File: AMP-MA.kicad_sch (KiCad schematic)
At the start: 51 parts, among them Q1 2N5484, Q12 2N5484, Q13 2N5484, Q2 2N5484, U2 LM1875

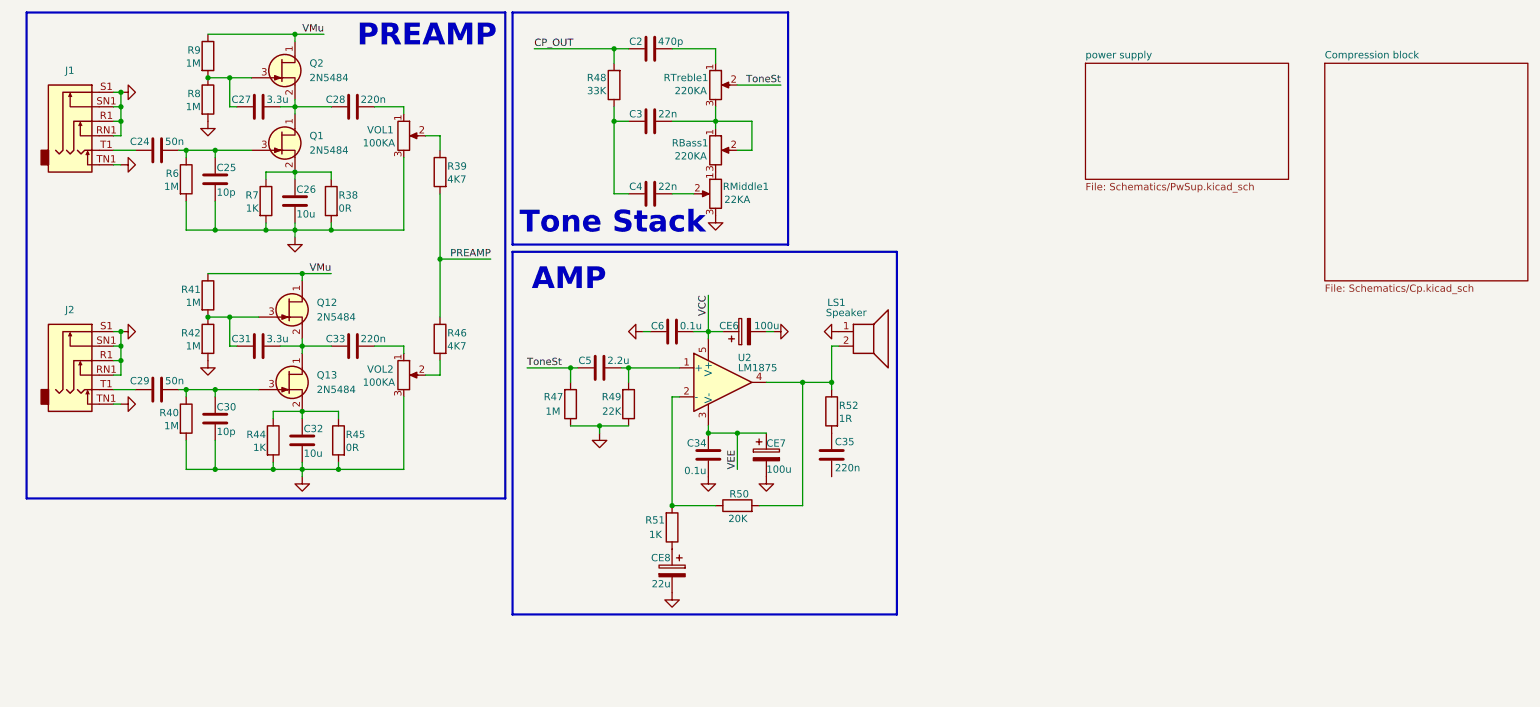
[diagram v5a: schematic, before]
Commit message: directory cleared, Schem upd
The input mixer changed from passive to active(TL072)
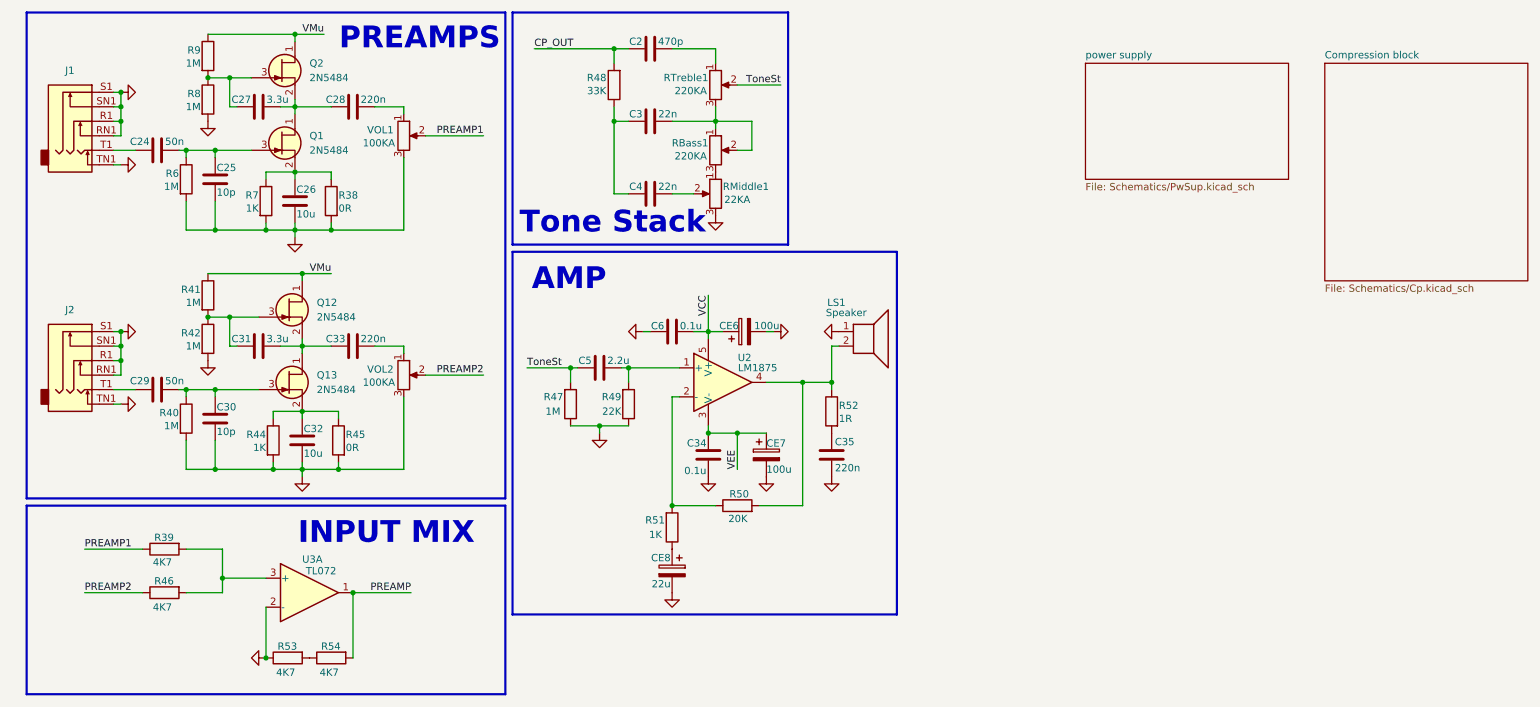
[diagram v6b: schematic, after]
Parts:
- added R53, R54: 4K7, Resistor_THT:R_Axial_DIN0207_L6.3mm_D2.5mm_P10.16mm_Horizontal, symbol Device:R
- added U3: TL072, symbol Amplifier_Operational:TL072
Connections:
- net GND: now also C35.2, R53.1, U3.2 (-)
- net PREAMP: now also R54.2, U3.1; no longer R39.2, R46.1
- net PREAMP1: now reaches R39.1, VOL1.2
- net at R46.2: now also R39.2, U3.3 (+); no longer VOL2.2
- new net: R53.2, R54.1
- new net PREAMP2: R46.1, VOL2.2
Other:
- note added: "INPUT MIX"
- note added: "PREAMPS"
- note removed: "PREAMP"

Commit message: Schem upd & added .gitignore
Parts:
- added J8: Conn_01x05_Socket, symbol Connector:Conn_01x05_Socket
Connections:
- net GND: now also CE7.1; no longer CE7.2
- net VCC: now also J8.4 (Pin_4)
- net VEE: now also CE7.2, J8.3 (Pin_3); no longer CE7.1
- net LM_OUT: now reaches LS1.2, R50.2, R52.1, U2.4
- net LM_OUT: now also J8.5 (Pin_5)
- net LM_IN-: now reaches R50.1, R51.2, U2.2 (-)
- net LM_IN-: now also J8.1 (Pin_1)
- net LM_IN+: now reaches C5.2, R49.2, U2.1 (+)
- net LM_IN+: now also J8.2 (Pin_2)
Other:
- note added: "LM_connector"
- moved on the sheet: C34, C35, C5, C6, CE6, CE7, CE8, LS1, R39, R46, R47, R49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

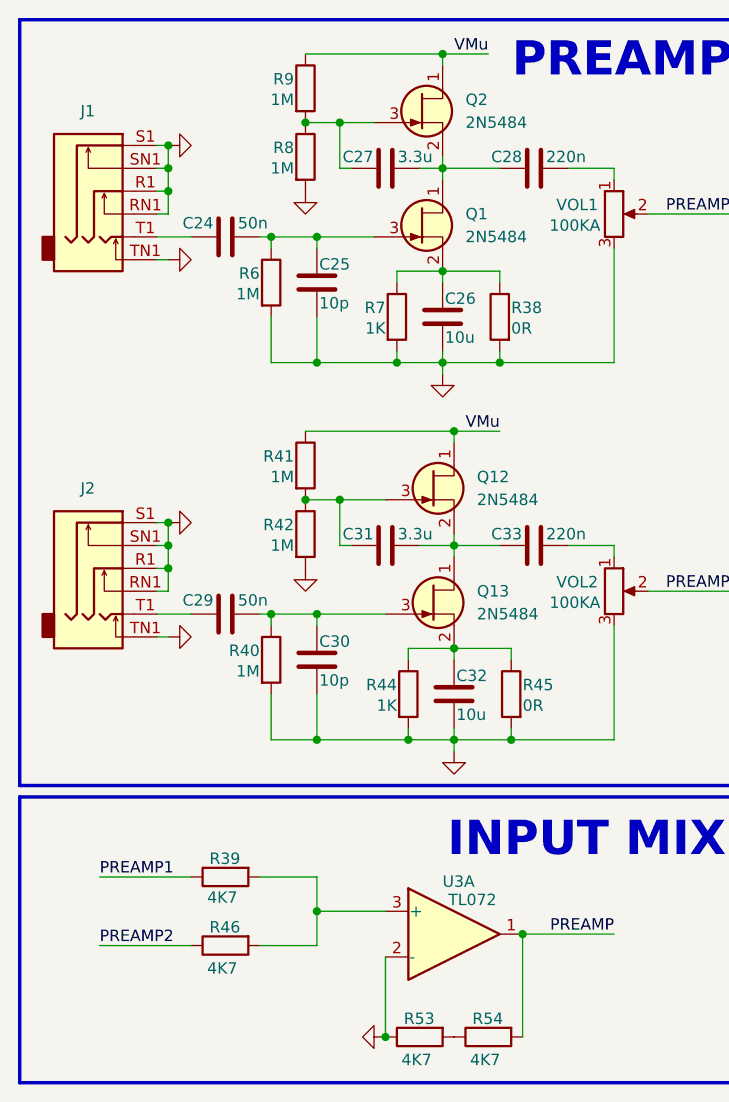
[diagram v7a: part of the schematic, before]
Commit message: Lib & Schematic upd
Jack connector symbol update. Made basic layout has been made
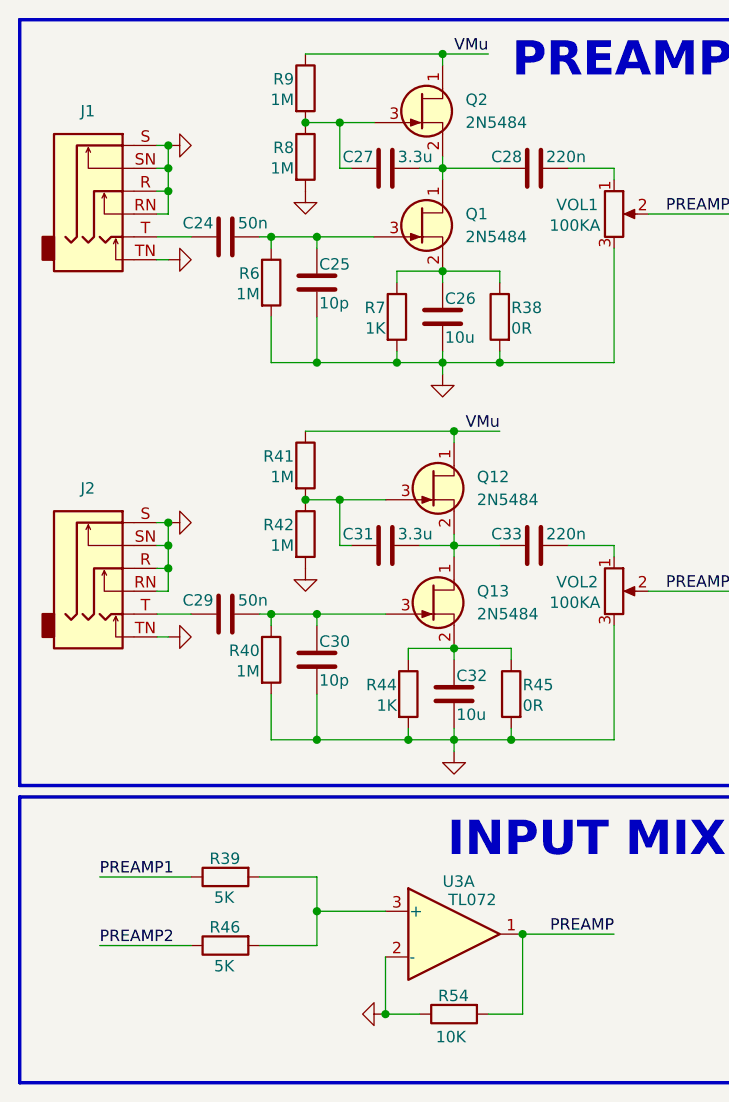
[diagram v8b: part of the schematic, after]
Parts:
- removed R53: 4K7, Resistor_THT:R_Axial_DIN0207_L6.3mm_D2.5mm_P10.16mm_Horizontal, symbol Device:R
- J8: footprint (none) -> Connector_JST:JST_PH_B5B-PH-K_1x05_P2.00mm_Vertical
- R39, R46: value 4K7 -> 5K
- R54: value 4K7 -> 10K
- RBass1, RMiddle1, RTreble1, VOL1, VOL2: footprint Potentiometer_THT:Potentiometer_Vishay_248BH-249BH_Single_Horizontal -> Potentiometer_THT:Potentiometer_Alps_RK09Y11_Single_Horizontal
- U3: footprint (none) -> Package_DIP:DIP-8_W7.62mm
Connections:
- net GND: now also J1.R, J1.RN, J1.S, J1.SN, J1.TN, J2.R, J2.RN, J2.S, J2.SN, J2.TN, R54.1; no longer J1.R1, J1.RN1, J1.S1, J1.SN1, J1.TN1, J2.R1, J2.RN1, J2.S1, J2.SN1, J2.TN1
- net at C29.1: now also J2.T; no longer J2.T1
- net at C24.1: now also J1.T; no longer J1.T1
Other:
- moved on the sheet: R54
